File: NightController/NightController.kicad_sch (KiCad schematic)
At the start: 10 parts

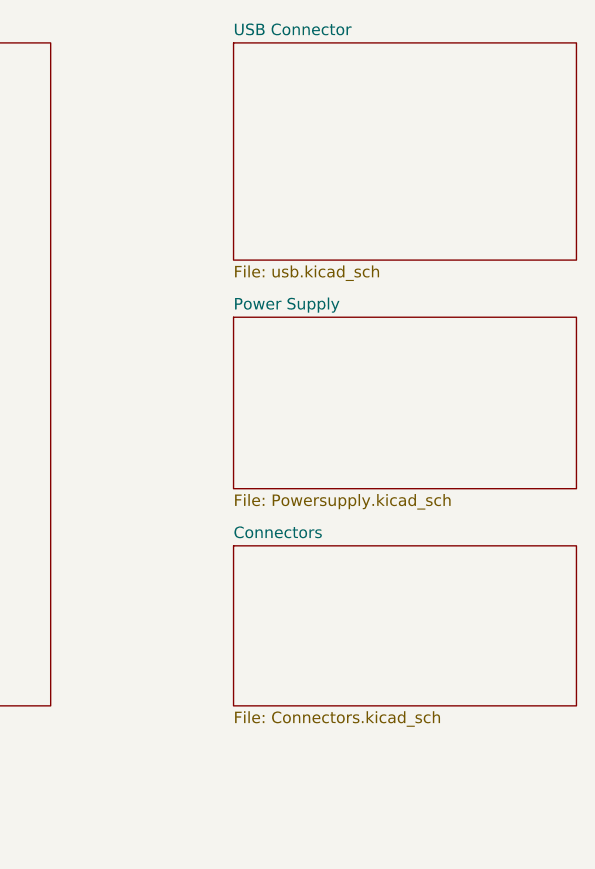
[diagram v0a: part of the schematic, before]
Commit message: update schematic
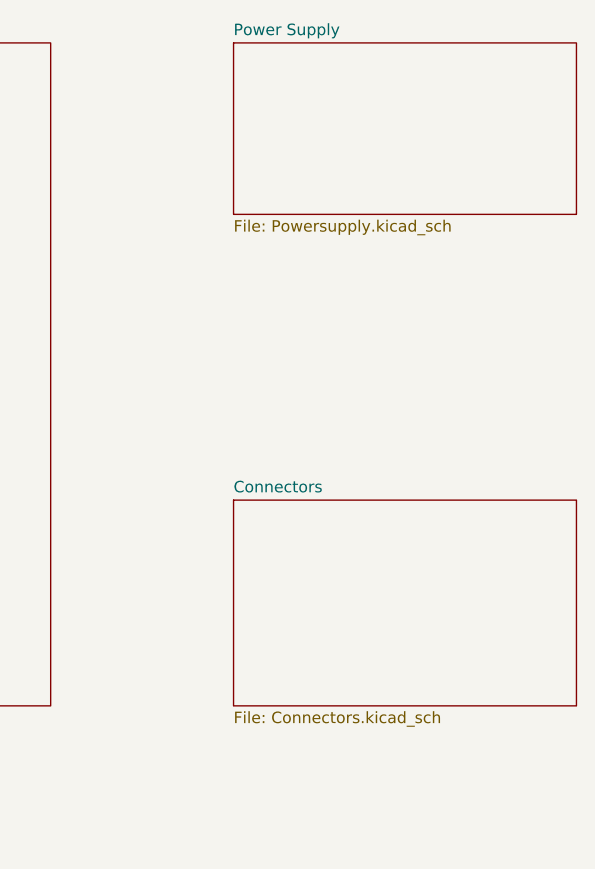
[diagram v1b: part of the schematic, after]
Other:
- removed sheet USB Connector
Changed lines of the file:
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@@
 	)
 	(sheet
-		(at 203.2 81.28)
+		(at 203.2 50.8)
 		(size 38.1 19.05)
 		(fields_autoplaced yes)
@@
 		)
 		(property "Sheetname" "Power Supply"
-			(at 203.2 80.5684 0)
+			(at 203.2 50.0884 0)
 			(effects
 				(font
@@
 		)
 		(property "Sheetfile" "Powersupply.kicad_sch"
-			(at 203.2 100.9146 0)
+			(at 203.2 70.4346 0)
 			(effects
 				(font
@@
 	)
 	(sheet
-		(at 203.2 106.68)
-		(size 38.1 17.78)
+		(at 203.2 101.6)
+		(size 38.1 22.86)
 		(fields_autoplaced yes)
 		(stroke
@@
 		)
 		(property "Sheetname" "Connectors"
-			(at 203.2 105.9684 0)
+			(at 203.2 100.8884 0)
 			(effects
 				(font
@@
 				)
 			)
-		)
-	)
-	(sheet
-		(at 203.2 50.8)
-		(size 38.1 24.13)
-		(fields_autoplaced yes)
-		(stroke
-			(width 0.1524)
-			(type solid)
-		)
-		(fill
-			(color 0 0 0 0.0000)
-		)
-		(property "Sheetname" "USB Connector"
-			(at 203.2 50.0884 0)
-			(effects
-				(font
-					(size 1.27 1.27)
-				)
-				(justify left bottom)
-			)
-		)
-		(property "Sheetfile" "usb.kicad_sch"
-			(at 203.2 75.5146 0)
-			(effects
-				(font
-					(size 1.27 1.27)
-				)
-				(justify left top)
-			)
-		)
-		(instances
-			(project "NightController"
-				(path "/84972824-c6a3-4762-8148-c4d5b5ede147"
-					(page "5")
-				)
-			)
